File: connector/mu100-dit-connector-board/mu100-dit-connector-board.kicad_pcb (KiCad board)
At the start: 2 copper layers, 37 x 14 mm, 8 parts, among them J1 Conn_01x17_Male, J2 Conn_01x17, J3 Conn_01x10_Female

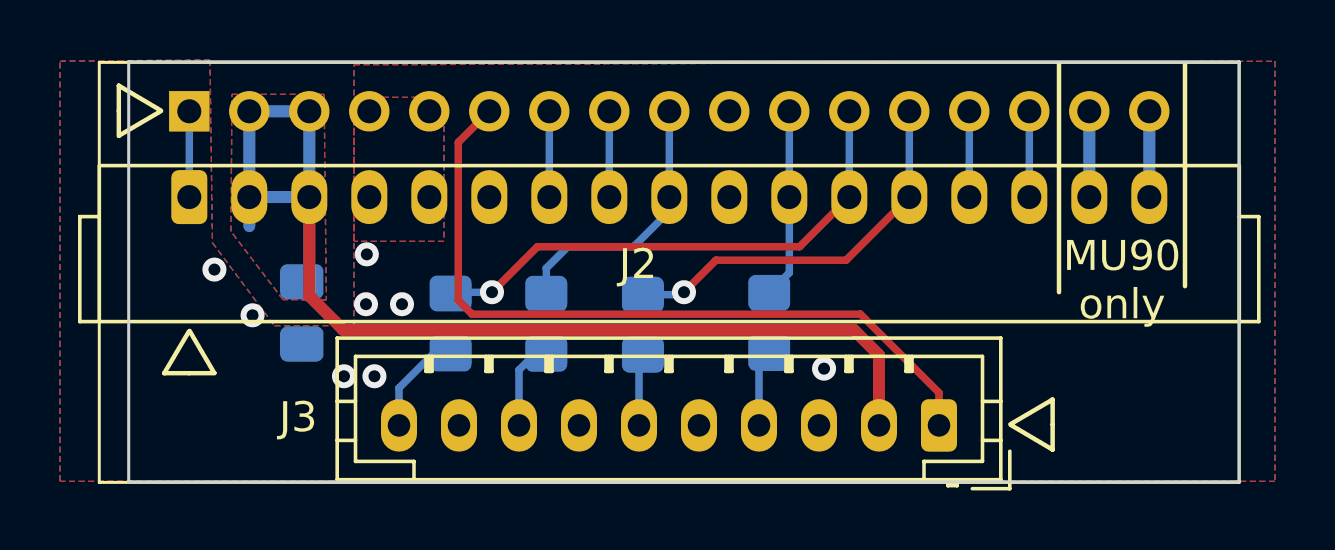
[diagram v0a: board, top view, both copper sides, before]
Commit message: Add reset circuit, remove need for reset
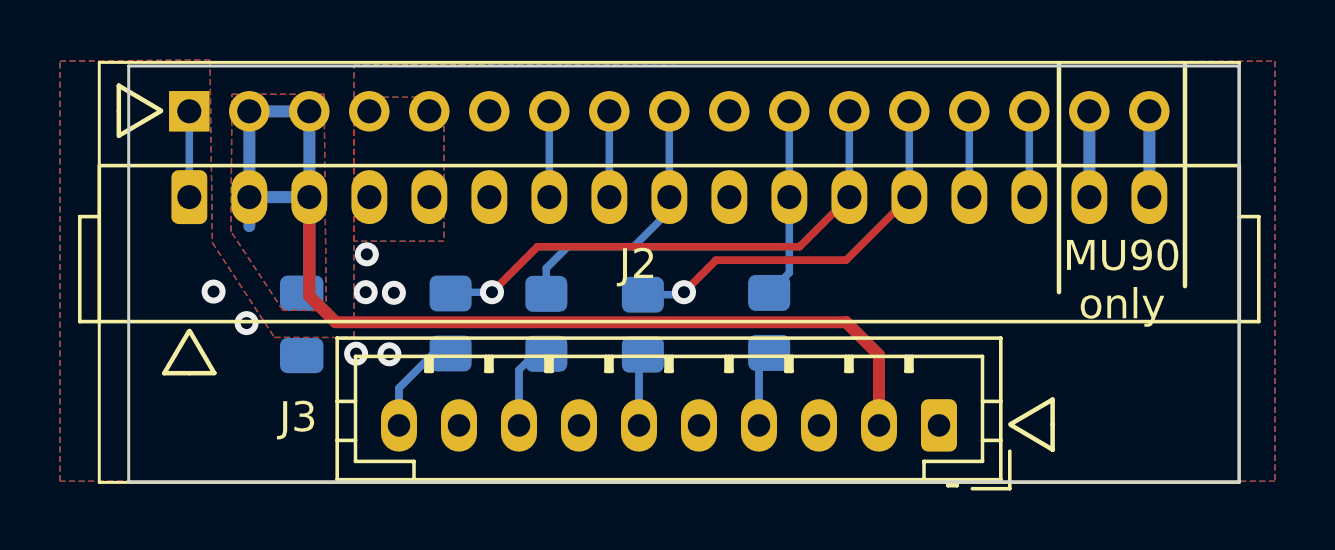
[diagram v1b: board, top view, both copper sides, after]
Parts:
- moved C1 0.38 mm to (69.5, 65.1)
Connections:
- J1 pad 6: /RESET -> unconnected-(J1-Pad6)
- J3 pad 1: /RESET -> unconnected-(J3-Pad1)
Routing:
- net /RESET: track 25.1 -> 0.00 mm
- net GND: vias 8 -> 7
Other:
- board size 37 x 14 mm -> 37 x 13.9 mm
- board text added: "NC"
- board text removed: "~{RST}"
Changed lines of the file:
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@@
   (net 2 "GND")
   (net 3 "/RER")
-  (net 4 "/RESET")
+  (net 4 "unconnected-(J1-Pad6)")
   (net 5 "/MEL00")
   (net 6 "/SYOD")
@@
   (net 20 "/BICK")
   (net 21 "/LRCK")
+  (net 22 "unconnected-(J3-Pad1)")
   (footprint "Connector_JST:JST_PH_B10B-PH-K_1x10_P2.00mm_Vertical" (layer "F.Cu")
     (at 90.7 68.44 180)
@@
     (fp_line (start -1.95 2.8) (end 19.95 2.8) (layer "F.Fab") (width 0.1))
     (pad "1" thru_hole roundrect (at 0 0 180) (size 1.2 1.75) (drill 0.75) (layers *.Cu *.Mask) (roundrect_rratio 0.2083333333)
-      (net 4 "/RESET") (pinfunction "Pin_1") (pintype "passive"))
+      (net 22 "unconnected-(J3-Pad1)") (pinfunction "Pin_1") (pintype "passive+no_connect"))
     (pad "2" thru_hole oval (at 2 0 180) (size 1.2 1.75) (drill 0.75) (layers *.Cu *.Mask)
       (net 1 "+5V") (pinfunction "Pin_2") (pintype "passive"))
@@
       (net 2 "GND") (pinfunction "Pin_5") (pintype "passive"))
     (pad "6" thru_hole oval (at 0 -10 270) (size 1.35 1.35) (drill 0.8) (layers *.Cu *.Mask)
-      (net 4 "/RESET") (pinfunction "Pin_6") (pintype "passive"))
+      (net 4 "unconnected-(J1-Pad6)") (pinfunction "Pin_6") (pintype "passive+no_connect"))
     (pad "7" thru_hole oval (at 0 -12 270) (size 1.35 1.35) (drill 0.8) (layers *.Cu *.Mask)
       (net 5 "/MEL00") (pinfunction "Pin_7") (pintype "passive"))
@@
   )
   (footprint "Capacitor_SMD:C_0805_2012Metric_Pad1.18x1.45mm_HandSolder" (layer "B.Cu")
-    (at 69.46 64.69 -90)
+    (at 69.46 65.074 -90)
     (descr "Capacitor SMD 0805 (2012 Metric), square (rectangular) end terminal, IPC_7351 nominal with elongated pad for handsoldering. (Body size source: IPC-SM-782 page 76, https://www.pcb-3d.com/wordpress/wp-content/uploads/ipc-sm-782a_amendment_1_and_2.pdf, https://docs.google.com/spreadsheets/d/1BsfQQcO9C6DZCsRaXUlFlo91Tg2WpOkGARC1WS5S8t0/edit?usp=sharing), generated with kicad-footprint-generator")
     (tags "capacitor handsolder")
@@
   (gr_line (start 93.108 68.434) (end 94.488 69.249) (layer "F.SilkS") (width 0.15))
   (gr_rect (start 62.025 54.3) (end 100.665 59.5) (layer "Cmts.User") (width 0.15) (fill none))
-  (gr_rect (start 63.69 56.32) (end 100.7 70.32) (layer "Edge.Cuts") (width 0.1) (fill none))
+  (gr_rect (start 63.69 56.46) (end 100.7 70.32) (layer "Edge.Cuts") (width 0.1) (fill none))
   (gr_text "+5V" (at 89 69.9) (layer "B.SilkS")
     (effects (font (size 0.5 0.5) (thickness 0.15)) (justify mirror))
@@
     (effects (font (size 0.5 0.5) (thickness 0.15)) (justify mirror))
   )
-  (gr_text "~{RST}" (at 90.8 70.0525) (layer "B.SilkS")
-    (effects (font (size 0.5 0.5) (thickness 0.15)) (justify mirror))
+  (gr_text "NC" (at 90.8 69.9) (layer "B.SilkS")
+    (effects (font (size 0.5 0.5) (thickness 0.125)) (justify mirror))
   )
   (gr_text "BICK" (at 76.7 69.9) (layer "B.SilkS")
@@
     (effects (font (size 1 1) (thickness 0.15)))
   )
+  (segment (start 69.71 60.83) (end 69.71 64.122) (width 0.4) (layer "F.Cu") (net 1))
+  (segment (start 69.71 64.122) (end 70.588 65) (width 0.4) (layer "F.Cu") (net 1))
+  (segment (start 87.606 65) (end 88.7 66.094) (width 0.4) (layer "F.Cu") (net 1))
   (segment (start 88.7 66.094) (end 88.7 68.44) (width 0.4) (layer "F.Cu") (net 1))
-  (segment (start 70.845031 65.257031) (end 87.863031 65.257031) (width 0.4) (layer "F.Cu") (net 1))
-  (segment (start 69.71 60.83) (end 69.71 64.122) (width 0.4) (layer "F.Cu") (net 1))
-  (segment (start 69.71 64.122) (end 70.845031 65.257031) (width 0.4) (layer "F.Cu") (net 1))
-  (segment (start 87.863031 65.257031) (end 88.7 66.094) (width 0.4) (layer "F.Cu") (net 1))
+  (segment (start 70.588 65) (end 87.606 65) (width 0.4) (layer "F.Cu") (net 1))
   (segment (start 67.71 57.97) (end 69.71 57.97) (width 0.4) (layer "B.Cu") (net 1))
   (segment (start 67.71 60.83) (end 69.71 60.83) (width 0.4) (layer "B.Cu") (net 1))
@@
   (segment (start 67.71 57.97) (end 67.71 61.7975) (width 0.4) (layer "B.Cu") (net 1))
   (segment (start 69.71 57.97) (end 69.71 60.83) (width 0.4) (layer "B.Cu") (net 1))
-  (via (at 70.866 66.802) (size 0.8) (drill 0.4) (layers "F.Cu" "B.Cu") (free) (net 2))
-  (via (at 67.818 64.77) (size 0.8) (drill 0.4) (layers "F.Cu" "B.Cu") (free) (net 2))
-  (via (at 72.8 64.4) (size 0.8) (drill 0.4) (layers "F.Cu" "B.Cu") (free) (net 2))
+  (via (at 71.27 66.05) (size 0.8) (drill 0.4) (layers "F.Cu" "B.Cu") (free) (net 2))
+  (via (at 67.62 65.03) (size 0.8) (drill 0.4) (layers "F.Cu" "B.Cu") (free) (net 2))
+  (via (at 72.53 64.02) (size 0.8) (drill 0.4) (layers "F.Cu" "B.Cu") (free) (net 2))
   (via (at 71.628 62.738) (size 0.8) (drill 0.4) (layers "F.Cu" "B.Cu") (free) (net 2))
-  (via (at 71.882 66.802) (size 0.8) (drill 0.4) (layers "F.Cu" "B.Cu") (free) (net 2))
-  (via (at 66.548 63.246) (size 0.8) (drill 0.4) (layers "F.Cu" "B.Cu") (free) (net 2))
-  (via (at 71.6 64.4) (size 0.8) (drill 0.4) (layers "F.Cu" "B.Cu") (free) (net 2))
-  (via (at 86.868 66.548) (size 0.8) (drill 0.4) (layers "F.Cu" "B.Cu") (free) (net 2))
+  (via (at 72.38 66.07) (size 0.8) (drill 0.4) (layers "F.Cu" "B.Cu") (free) (net 2))
+  (via (at 66.52 63.98) (size 0.8) (drill 0.4) (layers "F.Cu" "B.Cu") (free) (net 2))
+  (via (at 71.59 64) (size 0.8) (drill 0.4) (layers "F.Cu" "B.Cu") (free) (net 2))
   (segment (start 65.71 57.97) (end 65.71 60.83) (width 0.25) (layer "B.Cu") (net 3))
-  (segment (start 75.71 57.97) (end 74.676 59.004) (width 0.25) (layer "F.Cu") (net 4))
-  (segment (start 88.080294 64.732511) (end 88.247784 64.9) (width 0.25) (layer "F.Cu") (net 4))
-  (segment (start 88.247784 64.9) (end 90.7 67.352216) (width 0.25) (layer "F.Cu") (net 4))
-  (segment (start 74.676 59.004) (end 74.676 64.276) (width 0.25) (layer "F.Cu") (net 4))
-  (segment (start 74.676 64.276) (end 75.132511 64.732511) (width 0.25) (layer "F.Cu") (net 4))
-  (segment (start 75.132511 64.732511) (end 88.080294 64.732511) (width 0.25) (layer "F.Cu") (net 4))
-  (segment (start 90.7 67.352216) (end 90.7 68.44) (width 0.25) (layer "F.Cu") (net 4))
   (segment (start 77.71 57.97) (end 77.71 60.83) (width 0.25) (layer "B.Cu") (net 5))
   (segment (start 79.71 57.97) (end 79.71 60.83) (width 0.25) (layer "B.Cu") (net 6))
@@
     )
   )
+  (zone (net 0) (net_name "") (layers F&B.Cu) (hatch edge 0.508)
+    (connect_pads (clearance 0))
+    (min_thickness 0.254)
+    (keepout (tracks allowed) (vias allowed) (pads allowed ) (copperpour not_allowed) (footprints allowed))
+    (fill (thermal_gap 0.508) (thermal_bridge_width 0.508))
+    (polygon
+      (pts
+        (xy 98.54 61.41)
+        (xy 74.58 61.41)
+        (xy 74.58 56.51)
+        (xy 98.54 56.51)
+      )
+    )
+  )
   (zone (net 2) (net_name "GND") (layers F&B.Cu) (hatch edge 0.508)
     (connect_pads (clearance 0.508))
@@
         (xy 66.4 56.26)
         (xy 66.479963 62.351719)
-        (xy 68.549333 65.118564)
-        (xy 71.2 65.120006)
+        (xy 68.549121 65.50802)
+        (xy 71.199788 65.509462)
         (xy 71.2 56.42)
         (xy 101.9 56.3)
@@
     (polygon
       (pts
-        (xy 70.278294 64.260918)
-        (xy 68.834 64.24842)
+        (xy 70.275242 64.613627)
+        (xy 68.830948 64.601129)
         (xy 67.099799 61.976)
         (xy 67.131111 57.404)

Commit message: finish connector pcb
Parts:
- moved R4 0.92 mm to (73.5, 65.0)
- moved C1 0.83 mm to (68.6, 65.1)
- moved R3 0.37 mm to (81.2, 65.0)
- moved J3 0.35 mm to (90.7, 68.8)
- moved R2 0.27 mm to (77.3, 65.0)
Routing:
- net +5V: track 39.1 -> 49.3 mm
- net /WCLK: track 17.5 -> 18.4 mm
- net /LRCK: track 3.60 -> 2.94 mm
- net GND: track 0.00 -> 0.26 mm, vias 7 -> 5
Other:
- board size 37 x 13.9 mm -> 37 x 15 mm
- board text added: "+9VA"
- board text added: "100"
- board text added: "47"
- board text added: "5V"
- board text added: "AGND"
- board text added: "CK256 (MCLK)"
- board text added: "DACOL (SDAT)"
- board text added: "MELO0"
- board text added: "Molex connector on board"
- board text added: "QCLK (BCK)"
- board text added: "REA"
- board text added: "REB"
- board text added: "RER"
- board text added: "SYOD"
- board text added: "WCLK (LRCK)"
- board text added: "github.com/ nikitalita/ MU100-DIT"

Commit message: combine pcb projects
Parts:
- moved J1 23.7 mm to (79.1, 77.5), turned to 0 degrees
- moved J2 23.3 mm to (82.0, 77.5), turned to 90 degrees
- moved C1 20.0 mm to (86.2, 74.5), turned to 0 degrees
- moved J3 16.3 mm to (90.0, 52.5), turned to -90 degrees
- moved R4 13.5 mm to (86.2, 69.7), turned to 0 degrees
- moved R2 8.88 mm to (86.2, 65.8), turned to 0 degrees
- moved R1 6.98 mm to (86.2, 58.1), turned to 0 degrees
- moved R3 5.85 mm to (86.2, 62.0), turned to 0 degrees
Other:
- board size 37 x 15 mm -> 15 x 40 mm

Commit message: WIP
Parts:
- C1, J1, R1, R2, R3, R4: moved to F.Cu
- J2: value Conn_01x17 -> 51247 Molex; moved to B.Cu
- J3: value Conn_01x10_Female -> JST-PH_01x10_Socket; moved to B.Cu
- moved J1 28.2 mm to (80.0, 49.2)
- moved J2 28.2 mm to (82.8, 49.2), turned to -90 degrees
- moved C1 22.4 mm to (87.1, 52.2)
- moved J3 21.8 mm to (90.8, 74.2), turned to 90 degrees
- moved R4 12.7 mm to (87.0, 57.0)
- moved R1 10.5 mm to (87.0, 68.6)
- moved R2 5.03 mm to (87.0, 60.9)
- moved R3 2.87 mm to (87.0, 64.7)
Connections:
- J1 pad 10: unconnected-(J1-Pad10) -> Net-(J1-Pad10)
- J1 pad 6: unconnected-(J1-Pad6) -> Net-(J1-Pad6)
- J2 pad 10: unconnected-(J2-Pad10) -> Net-(J1-Pad10)
- J2 pad 6: unconnected-(J2-Pad6) -> Net-(J1-Pad6)
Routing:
- net Net-(J1-Pad6): track 0.00 -> 2.86 mm
- net Net-(J1-Pad10): track 0.00 -> 2.86 mm
- net +5V: track 49.3 -> 46.8 mm
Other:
- board size 15 x 40 mm -> 15.1 x 40 mm
- board text added: "16-17 MU90 only"
- board text added: "MU90/100R: Slots into Molex connector MU90/100: Soldered onto unpopulated header"
- board text removed: "MU90 only"
- board text removed: "Molex connector on board"
